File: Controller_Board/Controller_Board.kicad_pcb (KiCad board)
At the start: 2 copper layers, 118.1 x 55.9 mm, 48 parts, among them P1 USB_MICRO, U1 MCP73831, U2 LTC2941, U3 TCR2EF33, U4 ATMEGA32U4RC-A, U5 nRF24L01+, U6 I2C_DISPLAY, U7 NC7WZ07, Y1 ABLS-8.000MHZ-B4-T

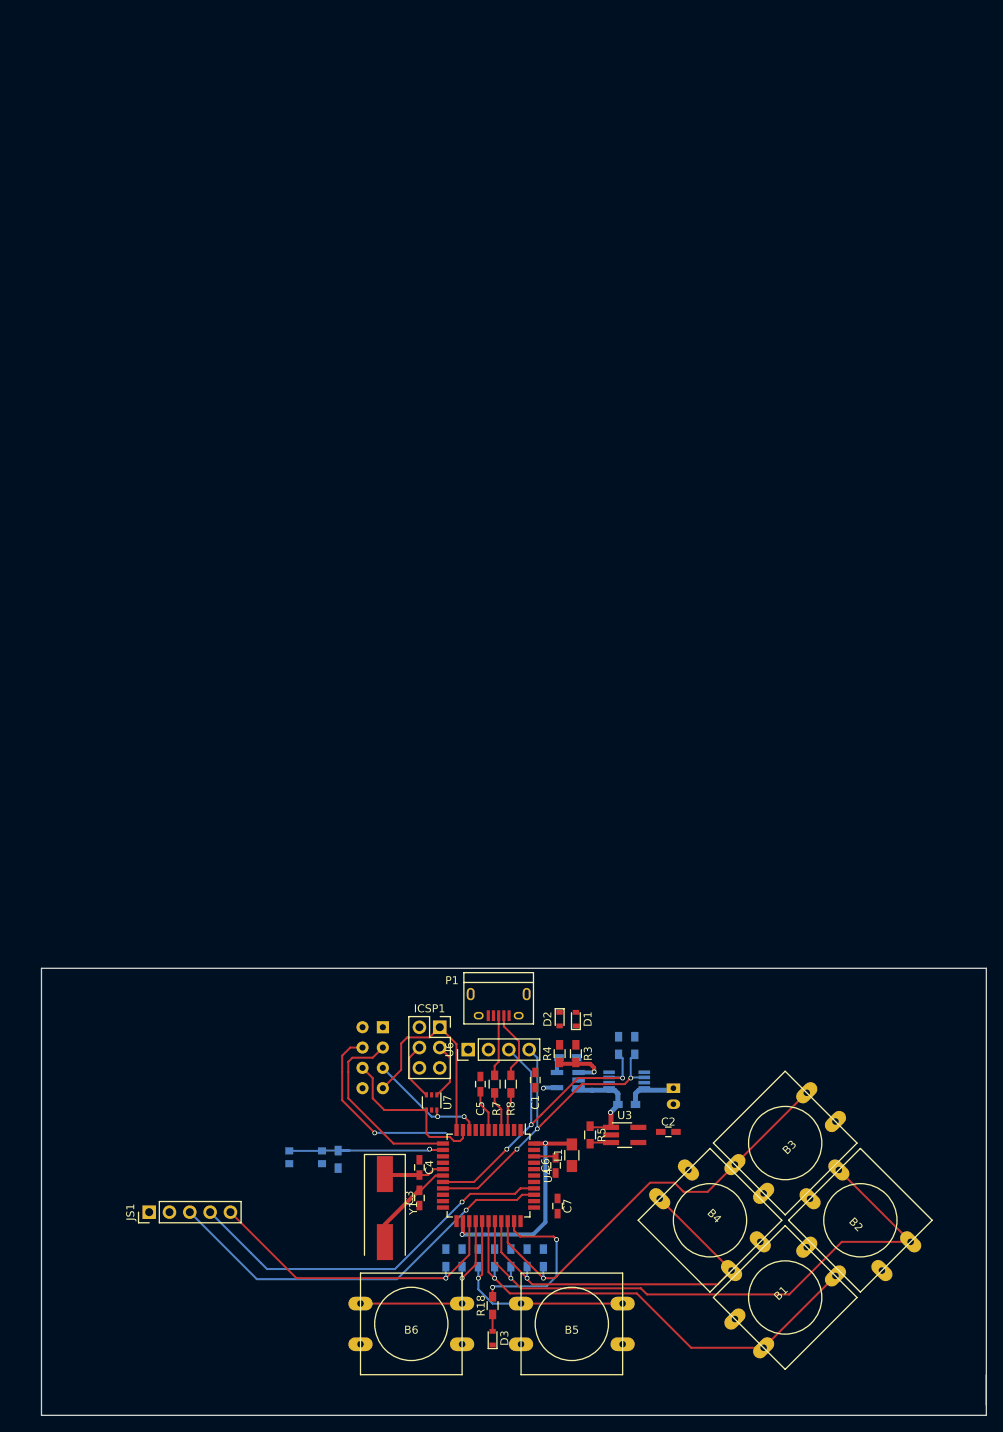
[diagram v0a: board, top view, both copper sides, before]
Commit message: Updated Controller Board with shoulder buttons, mounting holes, slightly altered pinout, second analog stick option, dual button footprints.... I really should have done this in stages...
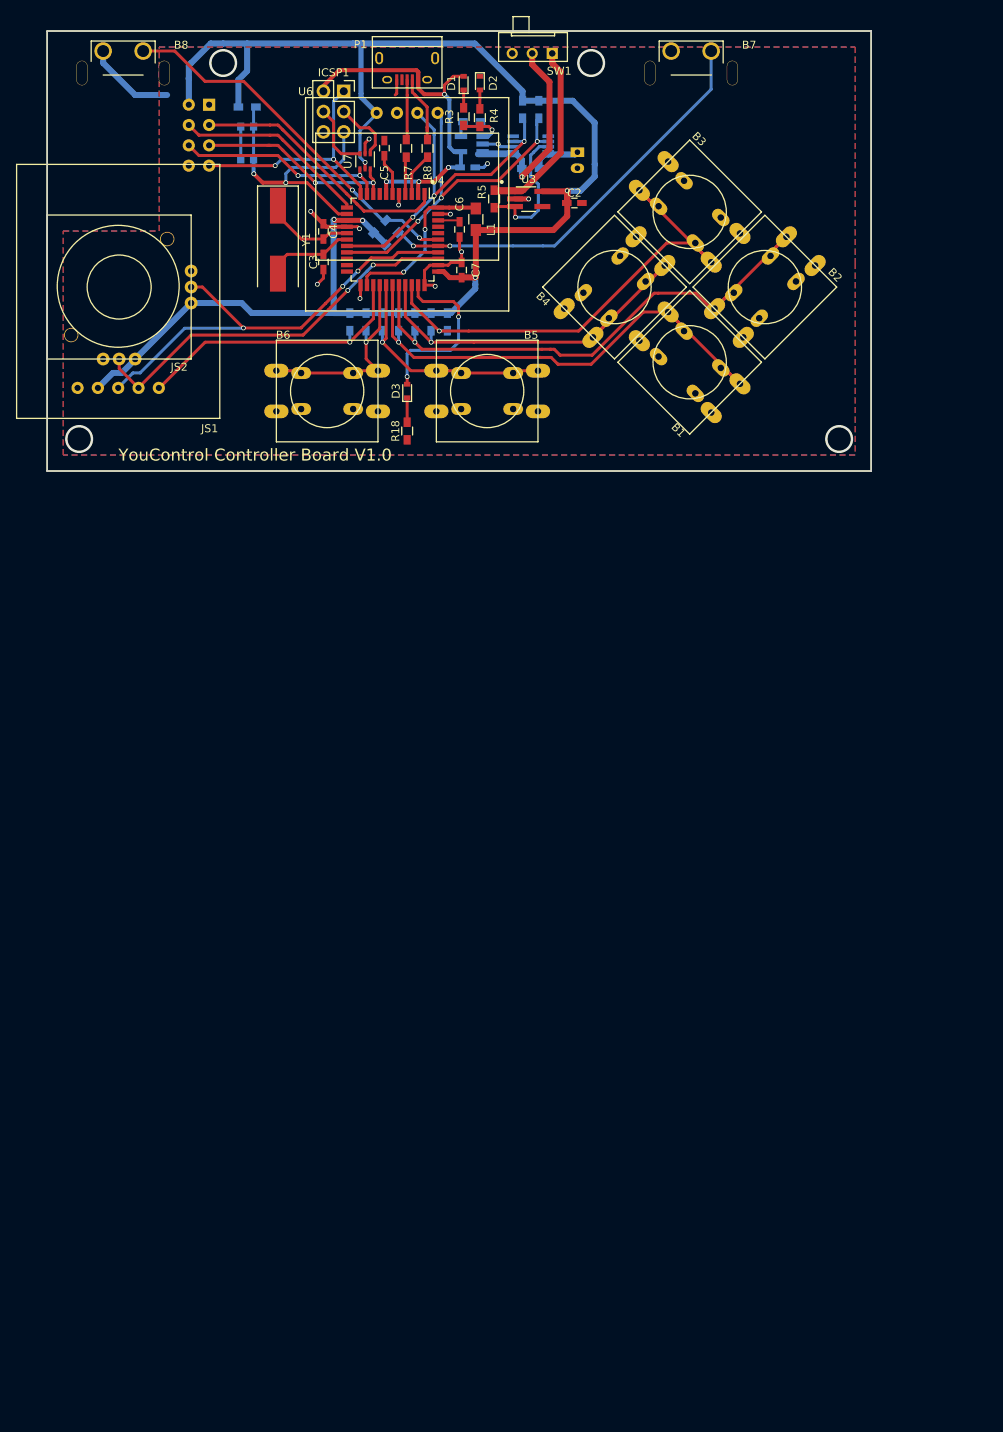
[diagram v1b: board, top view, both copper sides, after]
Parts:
- added B7: B3F-4000, YouControl:Button_Right_Angle, F.Cu at (113.0, 22.5)
- added B8: B3F-4000, YouControl:Button_Right_Angle, F.Cu at (42.0, 22.5)
- added JS2: JOYSTICK_Adafruit, YouControl:Joystick_Adafruit, F.Cu at (44.0, 52.0)
- added R19: 10k, Resistors_SMD:R_0603_HandSoldering, B.Cu at (78.1, 46.0)
- added R20: 10k, Resistors_SMD:R_0603_HandSoldering, B.Cu at (76.6, 44.5)
- added SW1: OS102011MA1QN1, YouControl:MHSS1105, F.Cu at (95.6, 22.8)
- B1, B2, B3, B4, B5, B6: footprint Buttons_Switches_ThroughHole:SW_PUSH-12mm -> YouControl:Button_Dual
- C1: moved to B.Cu
- JS1: footprint Socket_Strips:Socket_Strip_Straight_1x05_Pitch2.54mm -> YouControl:Joystick_PlayStation
- U6: footprint Socket_Strips:Socket_Strip_Straight_1x04_Pitch2.54mm -> YouControl:I2C_Screen
- moved R6 132.0 mm to (60.0, 29.5), turned to 180 degrees
- moved RESET1 127.0 mm to (60.0, 34.0), turned to 270 degrees
- moved Y1 121.8 mm to (63.8, 46.1)
- moved D3 118.9 mm to (80.0, 65.0)
- moved R3 118.0 mm to (87.1, 30.7)
- moved U7 117.9 mm to (74.7, 36.3)
- moved D1 117.8 mm to (87.1, 26.5)
- moved ICSP1 117.6 mm to (72.1, 27.5)
- moved R1 117.6 mm to (88.1, 31.3)
- moved R16 117.6 mm to (94.4, 29.8)
- moved R17 117.6 mm to (96.5, 29.8)
- moved U4 117.6 mm to (78.2, 46.1)
- moved C3 117.6 mm to (69.5, 48.9)
- moved C4 117.6 mm to (69.5, 45.1)
- moved C5 117.6 mm to (77.2, 34.6)
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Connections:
- D3 pad 1: GND -> Net-(D3-Pad1)
- D3 pad 2: Net-(D3-Pad2) -> /DEBUG_LED
- R18 pad 1: Net-(D3-Pad2) -> GND
- R18 pad 2: /DEBUG_LED -> Net-(D3-Pad1)
- R5 pad 1: +BATT -> Net-(R5-Pad1)
- R6 pad 1: Net-(R6-Pad1) -> /RESET
- RESET1 pad 2: Net-(R6-Pad1) -> /RESET
- U3 pad 1: +BATT -> Net-(R5-Pad1)
- U4 pad 1: /NRF_CSN -> /NRF_CE
- U4 pad 12: /NRF_CE -> /NRF_CSN
- U4 pad 13: Net-(R6-Pad1) -> /RESET
- U4 pad 36: /JOY_X -> /JOY_Y
- U4 pad 37: /JOY_Y -> /JOY_X
- U4 pad 38: Net-(U4-Pad38) -> /BUTTON_RB
- U4 pad 39: Net-(U4-Pad39) -> /BUTTON_LB
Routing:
- net +3V3: track 0.17 -> 219.8 mm, vias 0 -> 5
- net /BUTTON_RB: track 0.00 -> 52.6 mm, vias 0 -> 2
- net GND: track 0.00 -> 52.2 mm, vias 0 -> 12
- net +5V: track 1.79 -> 48.9 mm, vias 1 -> 4
- net /BUTTON_LB: track 0.00 -> 46.6 mm, vias 0 -> 2
- net /RESET: track 0.00 -> 34.7 mm, vias 0 -> 2
- net Net-(R5-Pad1): track 0.00 -> 27.1 mm
- net Net-(R6-Pad1): track 20.8 -> 0.00 mm, vias 1 -> 0
- net +BATT: track 14.4 -> 29.7 mm
- net Net-(R5-Pad2): track 2.88 -> 17.6 mm, vias 0 -> 1
- net /SCLK: track 15.5 -> 26.0 mm
- net /BUTTON_X: track 54.5 -> 63.9 mm
- net /NRF_CE: track 23.8 -> 32.9 mm
- net /BUTTON_A: track 58.8 -> 65.7 mm
- net Net-(L1-Pad2): track 27.5 -> 21.2 mm
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- added copper zone on B.Cu, net GND
- added copper zone on F.Cu, net GND
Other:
- board size 118.1 x 55.9 mm -> 103 x 55 mm
- board text added: "YouControl Controller Board V1.0"

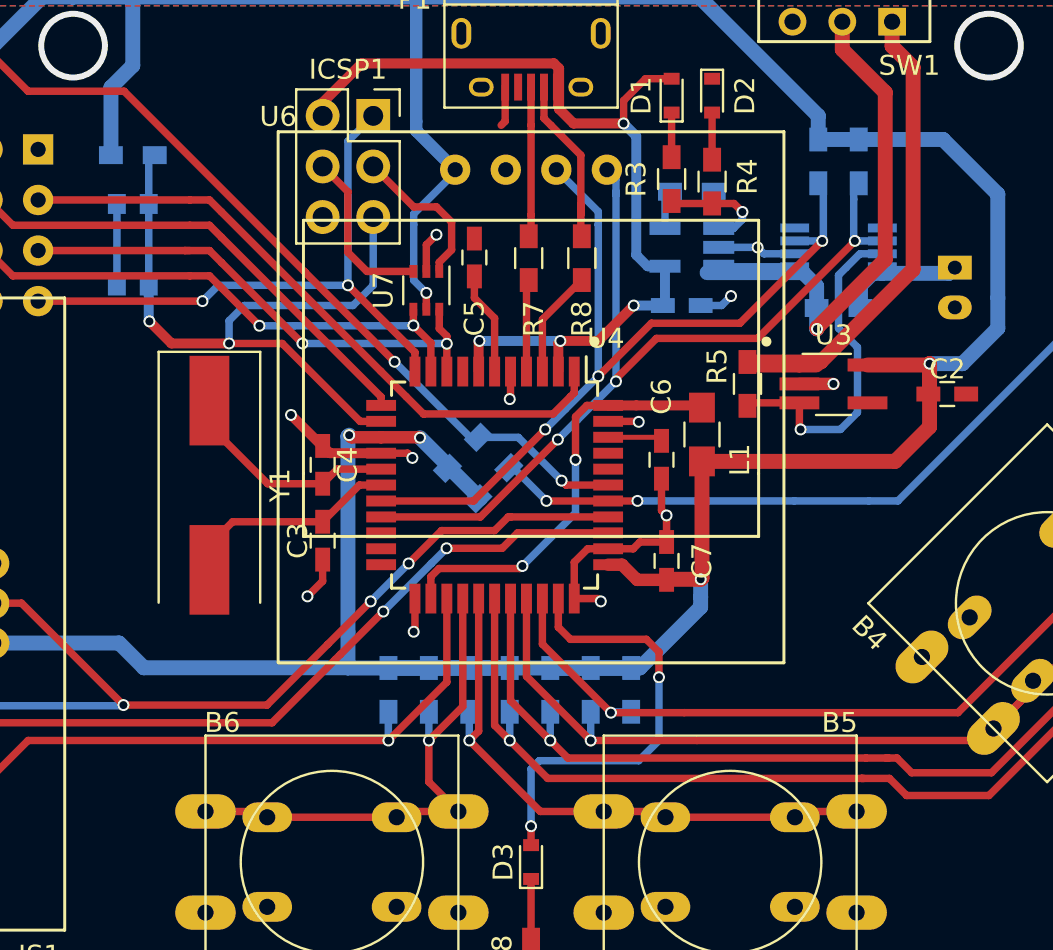
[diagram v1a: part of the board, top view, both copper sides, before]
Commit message: Updated Dongle and Controller boards, ready for fab
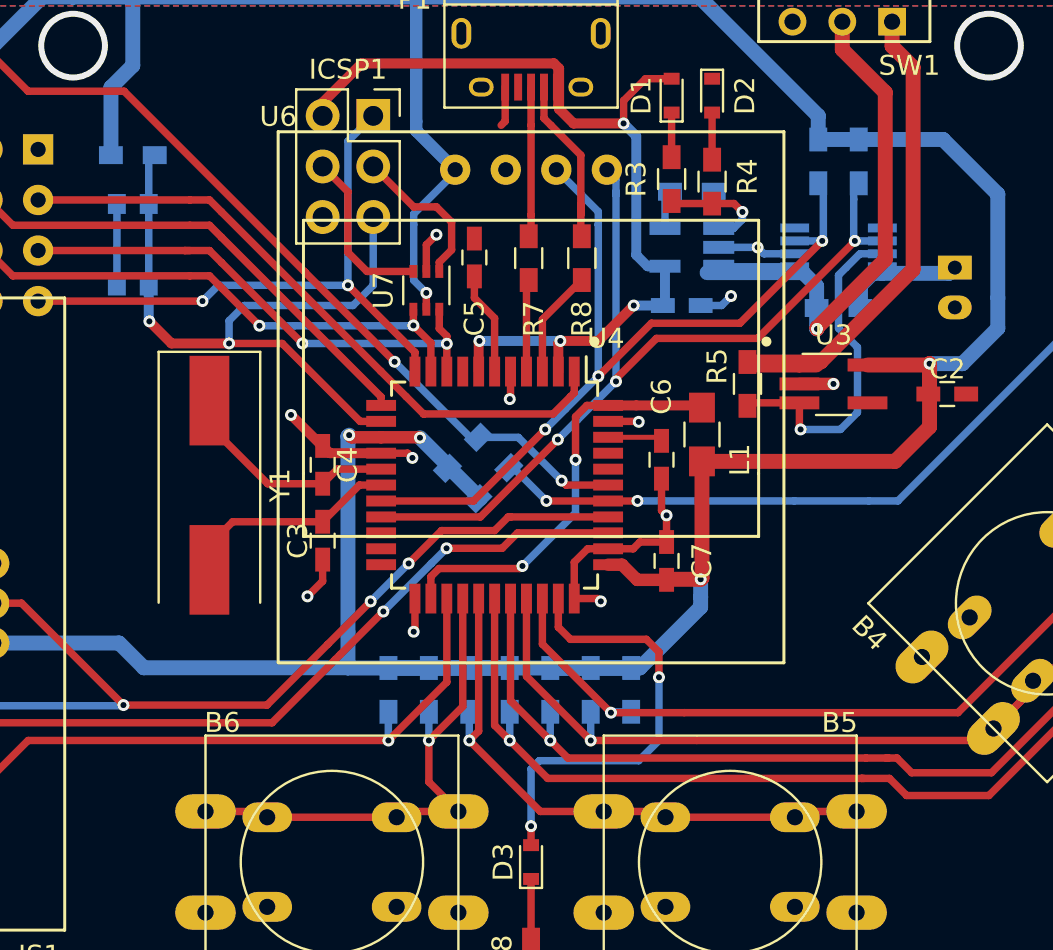
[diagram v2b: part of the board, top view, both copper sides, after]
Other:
- net class Default: via_drill 0.4 -> 0.3
